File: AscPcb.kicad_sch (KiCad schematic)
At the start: 31 parts, among them J1 12402012E212A, J2 B2B-PH-K-S, J3 Conn_01x10_Pin, SW1 TL3305AF260QG, SW2 TL3305AF260QG, U1 ESP32-C3-WROOM-02-N4, U2 BQ24040DSQR, U3 TLV75801PDRVR

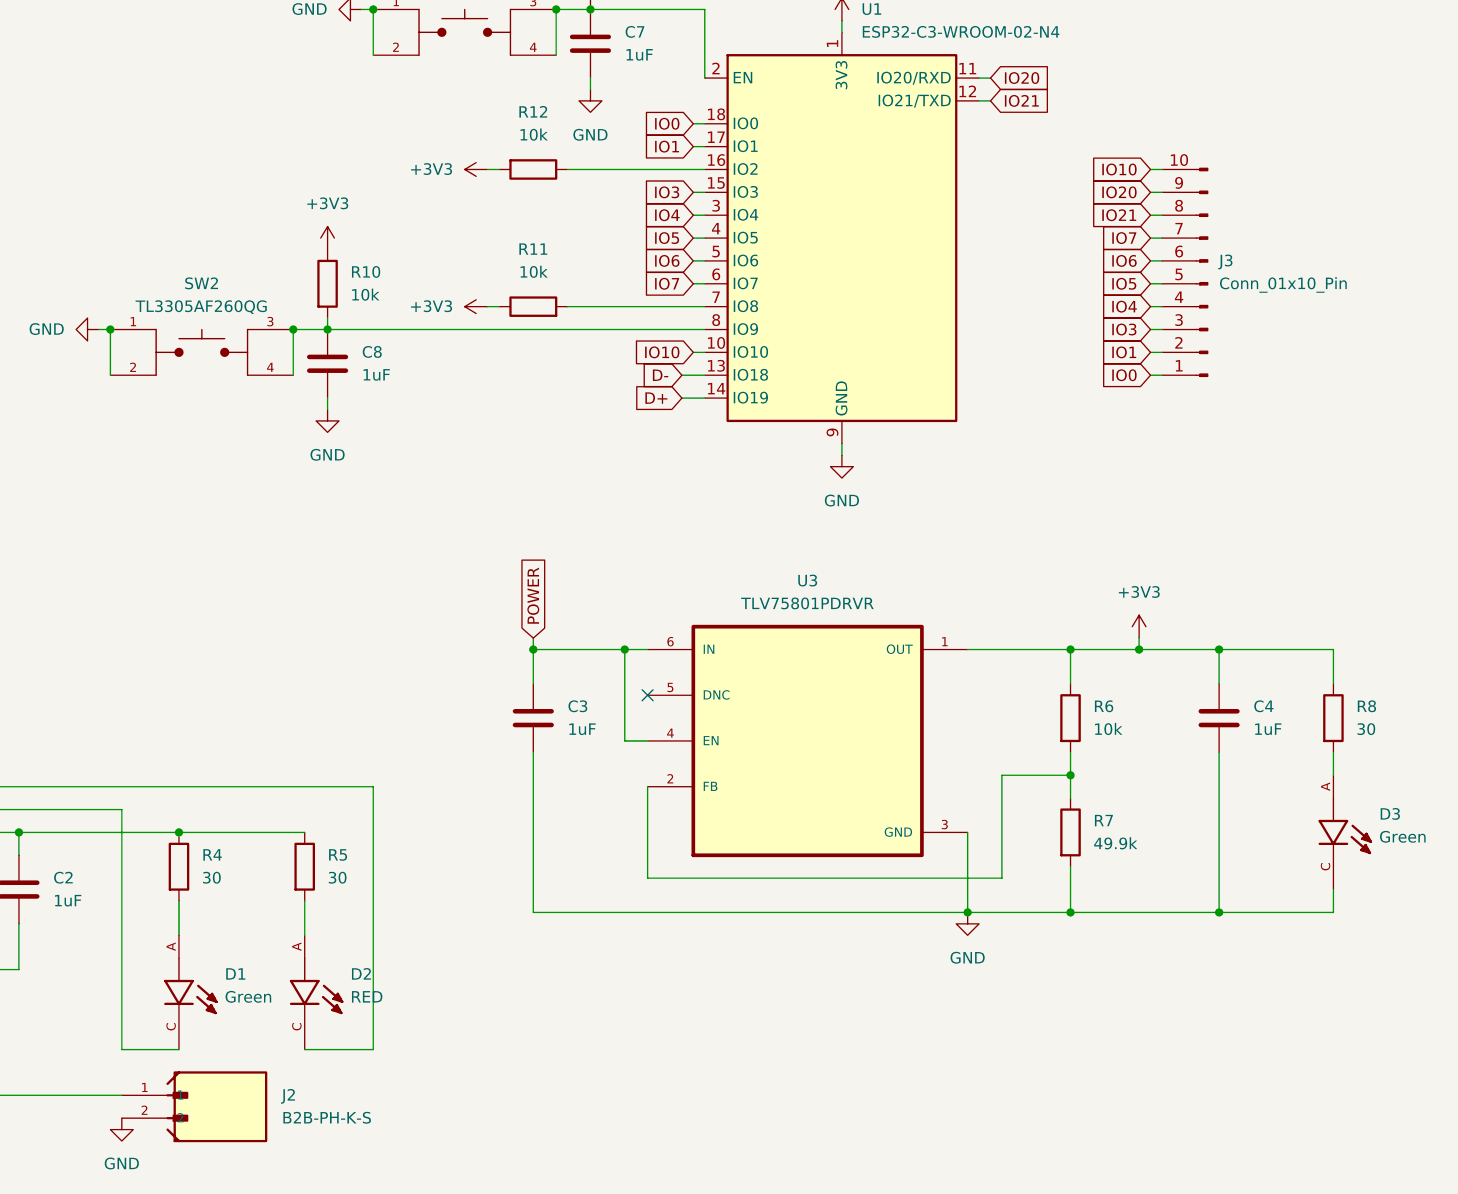
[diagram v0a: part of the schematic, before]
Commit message: new design: all components placed
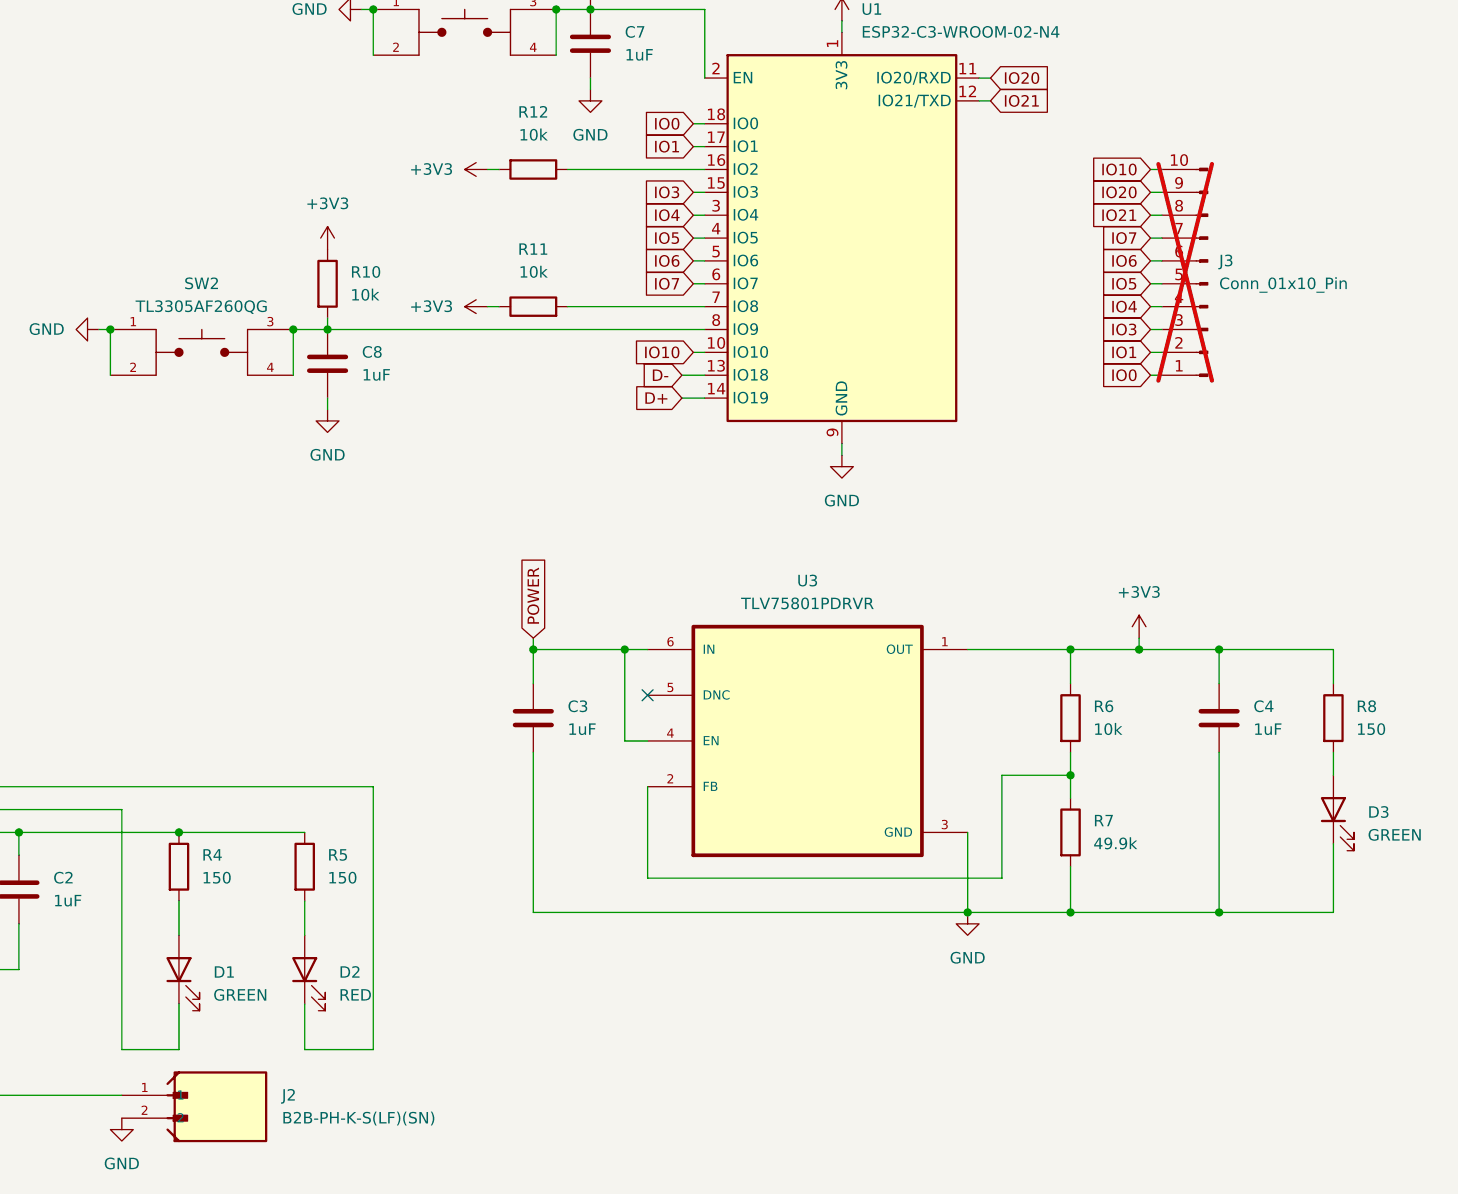
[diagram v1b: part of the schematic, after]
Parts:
- removed D1, D3: Green, L135_G525003500000:LED_L135-G525003500000, symbol L135-G525003500000:L135-G525003500000
- removed D2: RED, L135_G525003500000:LED_L135-G525003500000, symbol L135-G525003500000:L135-G525003500000
- added D1, D3: GREEN, LED_SMD:LED_0603_1608Metric, symbol Device:LED
- added D2: RED, LED_SMD:LED_0603_1608Metric, symbol Device:LED
- J2: value B2B-PH-K-S -> B2B-PH-K-S(LF)(SN); MPN B2B-PH-K-S -> B2B-PH-K-S(LF)(SN)
- J3: now not fitted; now left out of the parts list
- R4, R5, R8: value 30 -> 150; MPN RCP0603B30R0GEA -> CRCW0603150RFKEAC
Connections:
- net GND: now also D3.1 (K)
- net at R4.2: now also D1.2 (A)
- net at U2.5 (~{PG}): now also D1.1 (K)
- net at R8.2: now also D3.2 (A)
- net at U2.8 (~{CHG}): now also D2.1 (K)
- net at R5.2: now also D2.2 (A)

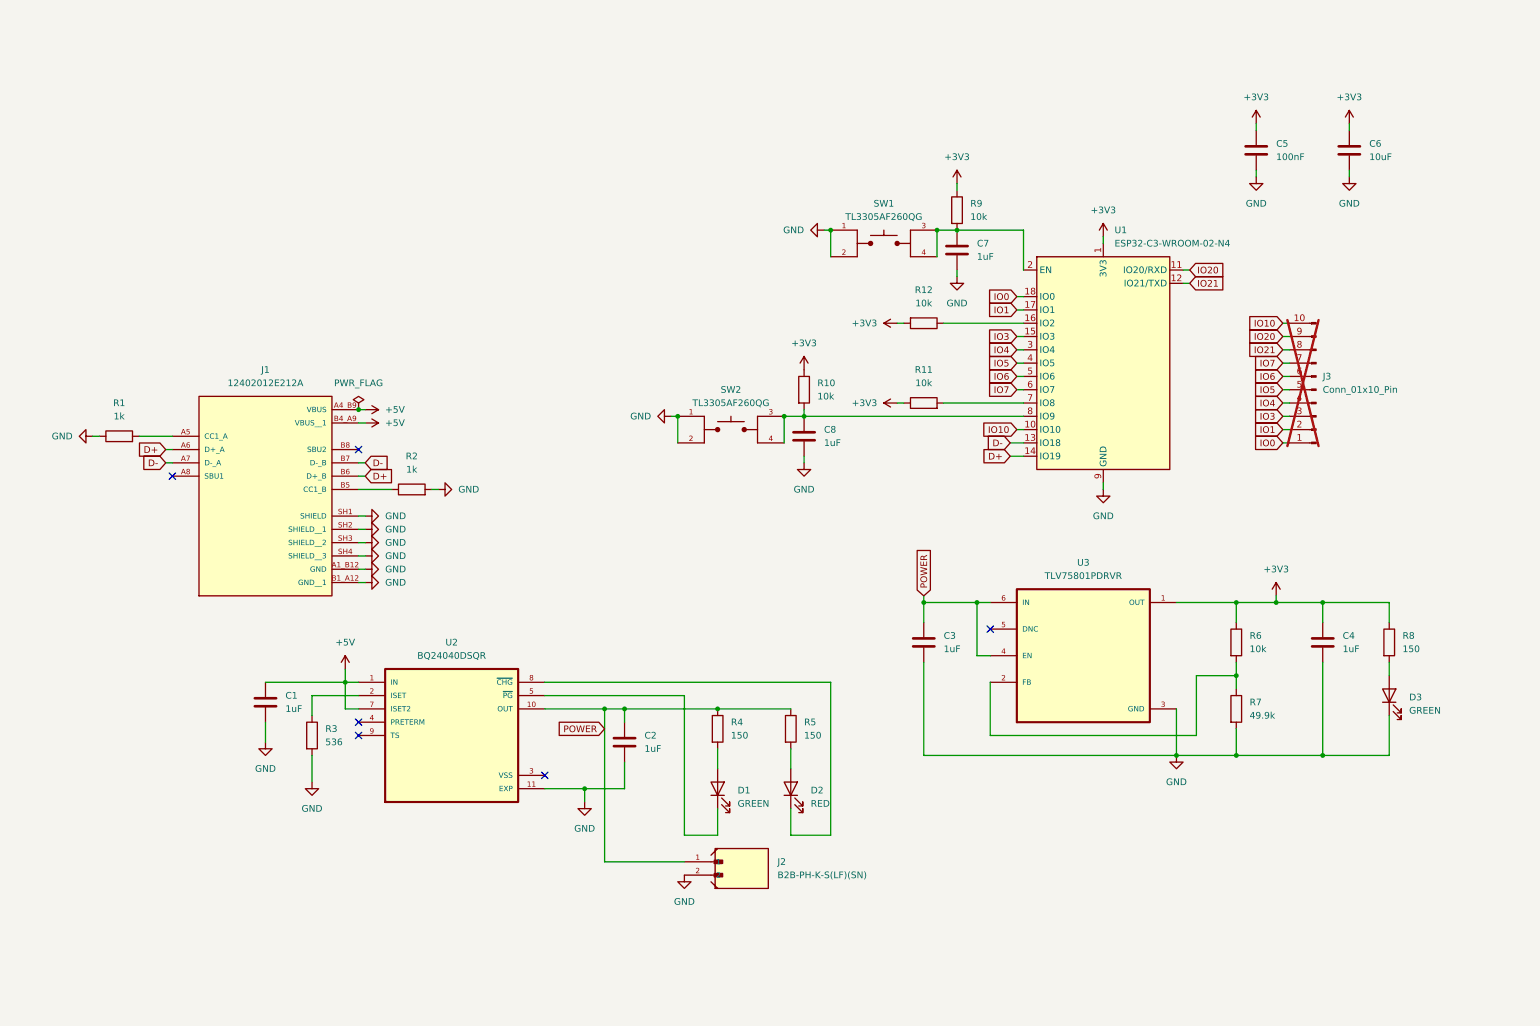
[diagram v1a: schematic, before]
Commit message: added bmi270 and ltc3625 and fixed some errors
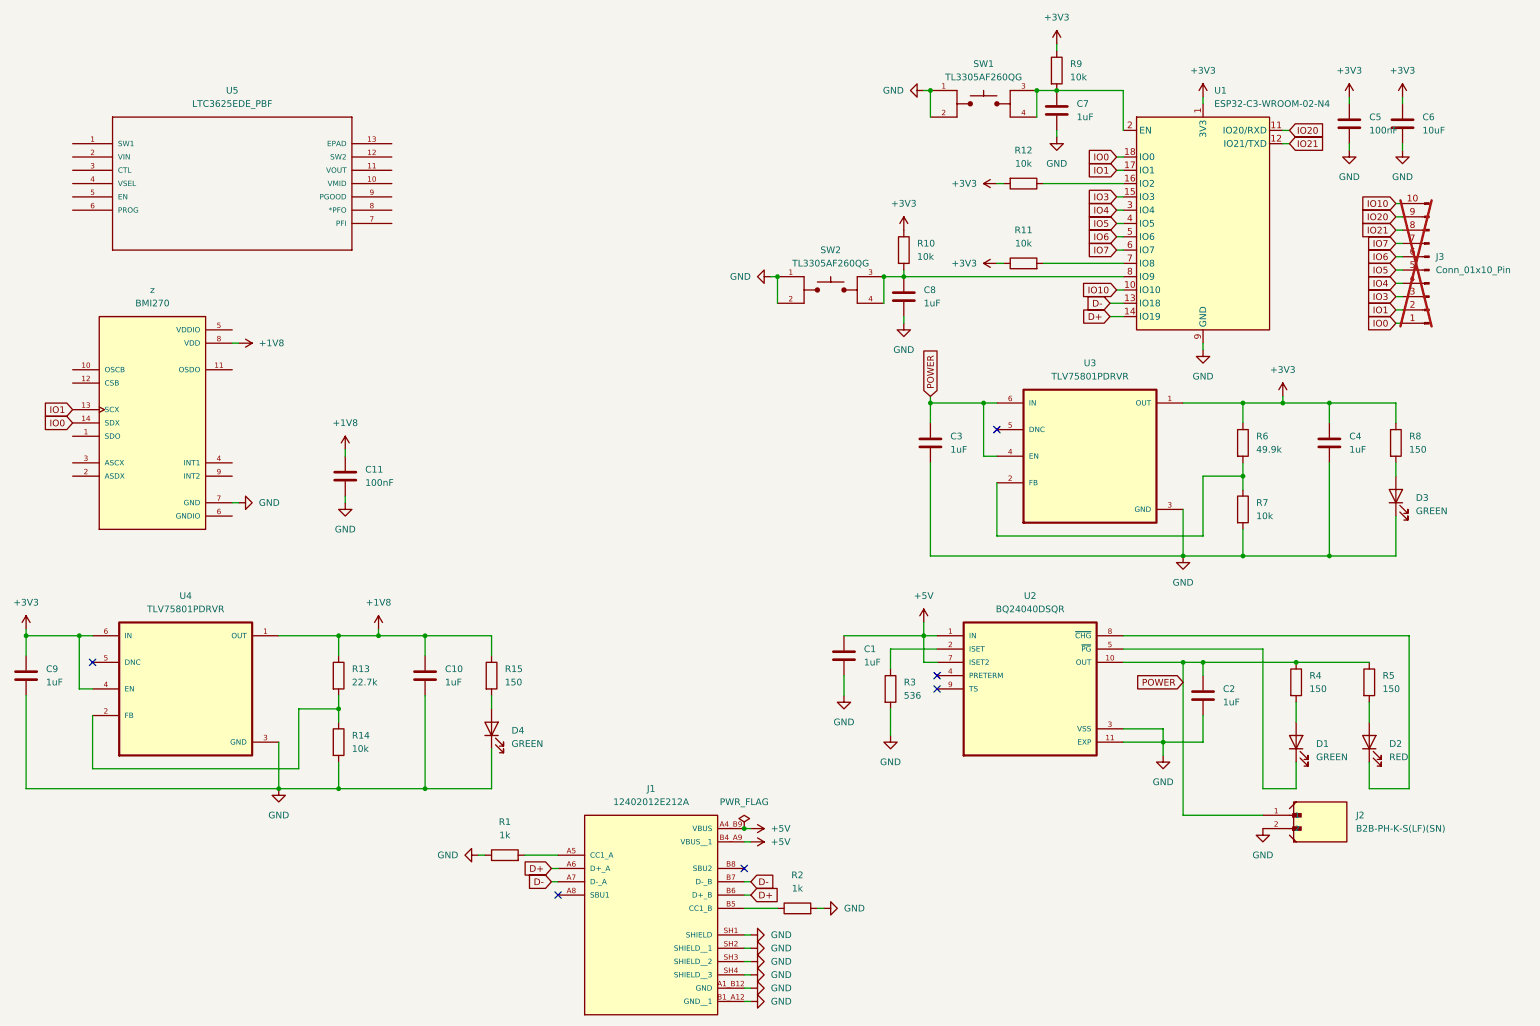
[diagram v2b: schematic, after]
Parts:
- added C10, C9: 1uF, Capacitor_SMD:C_0603_1608Metric, symbol Device:C
- added C11: 100nF, Capacitor_SMD:C_0603_1608Metric, symbol Device:C
- added D4: GREEN, LED_SMD:LED_0603_1608Metric, symbol Device:LED
- added R13: 22.7k, Resistor_SMD:R_0603_1608Metric, symbol Device:R
- added R14: 10k, Resistor_SMD:R_0603_1608Metric, symbol Device:R
- added R15: 150, Resistor_SMD:R_0603_1608Metric, symbol Device:R
- added U4: TLV75801PDRVR, TLV75801PDRVR:SON65P200X200X80-7N, symbol TLV75801PDRVR:TLV75801PDRVR
- added U5: LTC3625EDE_PBF, LTC3625EDE_PBF:DFN-12_DE, symbol LTC3625EDE_PBF:LTC3625EDE_PBF
- added z: BMI270, BMI270:XDCR_BMI270, symbol BMI270:BMI270
- J3: footprint Connector_PinHeader_1.00mm:PinHeader_1x10_P1.00mm_Vertical -> Connector_PinHeader_2.54mm:PinHeader_1x10_P2.54mm_Vertical
- renumbered R7 to R6, R6 to R7
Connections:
- net +3V3: now also R6.1, C9.1, U4.4 (EN), U4.6 (IN); no longer R7.1
- net GND: now also R7.2, U2.3 (VSS), C10.2, C11.2, C9.2, D4.1 (K), R14.2, U4.3 (GND), z.7 (GND); no longer R6.2
- net IO0: now also z.14 (SDX)
- net IO1: now also z.13 (SCX)
- new net: R13.2, R14.1, U4.2 (FB)
- new net: R6.2, R7.1, U3.2 (FB)
- new net: D4.2 (A), R15.2
- new net +1V8: C10.1, C11.1, R13.1, R15.1, U4.1 (OUT), z.8 (VDD)
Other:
- moved on the sheet: C1, C2, C3, C4, C5, C6, C7, C8, D1, D2, D3, J1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

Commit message: super cap charger fix some errors and basic setup for motor control
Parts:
- removed U4: TLV75801PDRVR, TLV75801PDRVR:SON65P200X200X80-7N, symbol TLV75801PDRVR:TLV75801PDRVR
- added C12, C13: 22uF, Capacitor_SMD:C_0603_1608Metric, symbol Device:C
- added C14: 10uF, Capacitor_SMD:C_0603_1608Metric, symbol Device:C
- added C15, C16: 100F, Capacitor_THT:CP_Radial_D22.0mm_P10.00mm_SnapIn, symbol Device:C
- added D5: D, symbol Device:D
- added H1, H2, H3, H4: MountingHole_Pad, MountingHole:MountingHole_3.2mm_M3_Pad, symbol Mechanical:MountingHole_Pad
- added J4: Conn_01x06_Pin, Connector_PinHeader_2.54mm:PinHeader_1x06_P2.54mm_Vertical, symbol Connector:Conn_01x06_Pin
- added J5, J9: Screw_Terminal_01x02, TerminalBlock_CUI:TerminalBlock_CUI_TB007-508-02_1x02_P5.08mm_Horizontal, symbol Connector:Screw_Terminal_01x02
- added J6, J7: Conn_01x02_Pin, symbol Connector:Conn_01x02_Pin
- added J8: Conn_01x03_Pin, Connector_PinHeader_2.54mm:PinHeader_1x03_P2.54mm_Vertical, symbol Connector:Conn_01x03_Pin
- added L1: 3.3uH, Inductor_SMD:L_0805_2012Metric, symbol Device:L
- added L2, L3: 3.3uH, DR73-3R3-R:DR73-3R3-R_EAT, symbol Device:L
- added Q1: Q_NMOS_DGS, symbol Transistor_FET:Q_NMOS_DGS
- added R16: 10k, Resistor_SMD:R_0603_1608Metric, symbol Device:R
- added R17: 150, Resistor_SMD:R_0603_1608Metric, symbol Device:R
- added R18: 61.9k, Resistor_SMD:R_0603_1608Metric, symbol Device:R
- added U8: AP62300TWU, Package_TO_SOT_SMD:TSOT-23-6, symbol Regulator_Switching:AP62300TWU
- C10: value 1uF -> 220nF; MPN CL10B105KP8NNNC -> CGA3E3X7R1H224K080AB
- C6: MPN T58MM106M6R3C0500 -> CL10A106KQ8NNNC
- C9: value 1uF -> 10uF; MPN CL10B105KP8NNNC -> CL10X106MO8NRNC
- J3: now fitted; now in the parts list
- R13: value 22.7k -> 10k; MPN CRCW060322K6FKEA -> RC0603FR-0710KL
- R15: value 150 -> 33.2k; footprint Resistor_SMD:R_0603_1608Metric -> Resistor_SMD:R_0805_2012Metric; MPN CRCW0603150RFKEAC -> CRCW080533K2FKEA
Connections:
- net +3V3: now also C11.1, R13.1, R14.1, z.12 (CSB), z.5 (VDDIO), z.8 (VDD); no longer C9.1
- net GND: now also C9.1, U5.13 (EPAD), U5.3 (CTL), U5.4 (VSEL), z.6 (GNDIO), C12.2, C13.2, C14.1, C16.1, J5.1 (Pin_1), Q1.3 (S), R16.2, R18.2, U8.1 (GND); no longer C10.2, C9.2, R14.2
- net IO0: now also R14.2
- net IO1: now also R13.2
- net IO3: now also Q1.2 (G)
- net POWER: now also J6.1 (Pin_1), J7.1 (Pin_1); no longer C2.1, J2.1, R4.1, R5.1, U2.10 (OUT)
- net at D4.2 (A): now also R17.2; no longer R15.2
- net at U5.1 (SW1): now also L2.1
- net at U5.10 (VMID): now also C15.1, C16.2, L2.2, L3.2
- net at U5.11 (VOUT): now also C15.2, J7.2 (Pin_2)
- net at U5.12 (SW2): now also L3.1
- net 3V3LTC: now reaches U5.2 (VIN)
- net 3V3LTC: now also R15.1, U5.5 (EN), C12.1, C13.1, C14.2, L1.2, R17.1
- net at U5.6 (PROG): now also R18.1
- net at U5.7 (PFI): now also J8.1 (Pin_1)
- net at U5.8 (*PFO): now also J8.2 (Pin_2)
- net at U5.9 (PGOOD): now also J8.3 (Pin_3)
- net SA0: now reaches z.1 (SDO)
- net OSCB: now reaches z.10 (OSCB)
- net OSCB: now also J4.2 (Pin_2)
- net OSDO: now reaches z.11 (OSDO)
- net OSDO: now also J4.1 (Pin_1)
- net ASDX: now reaches z.2 (ASDX)
- net ASDX: now also J4.6 (Pin_6)
- net ASCX: now reaches z.3 (ASCX)
- net ASCX: now also J4.5 (Pin_5)
- net INT1: now reaches z.4 (INT1)
- net INT1: now also J4.3 (Pin_3)
- net INT2: now reaches z.9 (INT2)
- net INT2: now also J4.4 (Pin_4)
- removed net +1V8: C10.1, C11.1, R13.1, R15.1, z.8 (VDD)
- new net: C2.1, J2.1, J6.2 (Pin_2), R4.1, R5.1, U2.10 (OUT)
- new net: C10.1, L1.1, U8.2 (SW)
- new net: C10.2, U8.6 (BST)
- new net: D5.2 (A), J9.1 (Pin_1), Q1.1 (D)
- new net: R15.2, R16.1, U8.4 (FB)
- new net +12V: C9.2, D5.1 (K), J5.2 (Pin_2), J9.2 (Pin_2), U8.3 (IN), U8.5 (EN)
- no-connect marks 6 -> 9
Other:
- note added: "Wenn nicht minimal 3.3V ausgegeben werden können, funktioniert die Schaltung nicht mehr, also LED als Indikation. Als schlussendliche Lösung: Buck-Boost anstatt Linearem Regulator und Monitoring durch esp"
- moved on the sheet: C1, C11, C2, C3, C4, C5, C6, C7, C8, D1, D2, D3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
